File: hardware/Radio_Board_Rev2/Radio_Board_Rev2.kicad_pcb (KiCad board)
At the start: 2 copper layers, 100 x 65.5 mm, 20 parts, among them IC1 MAX7219CNG, J1 Conn_01x02_Socket, SW1 SW_DIP_x01, SW2 SW_DIP_x01, SW3 SW_DIP_x01, U1 ESP32-DEVKIT-V1, U3 MIC5219-3.3YM5

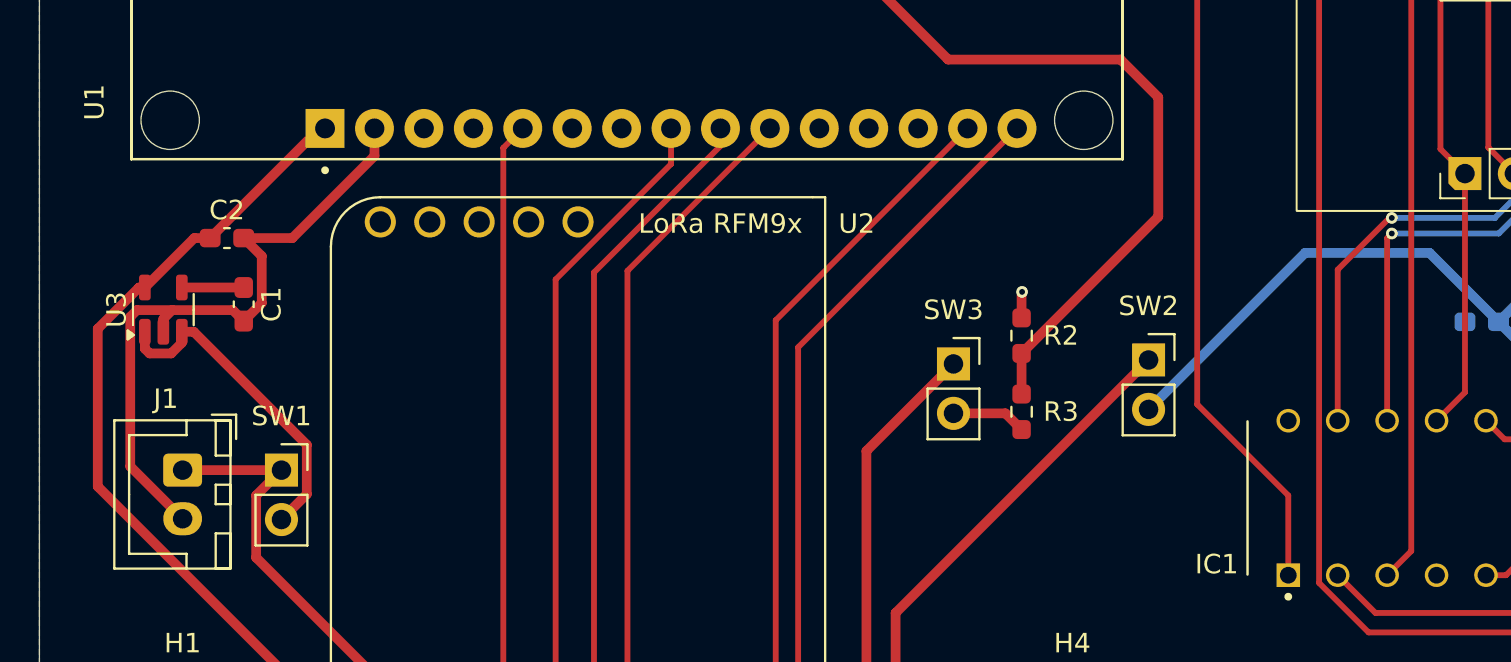
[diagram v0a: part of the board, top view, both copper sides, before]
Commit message: Add datasheets
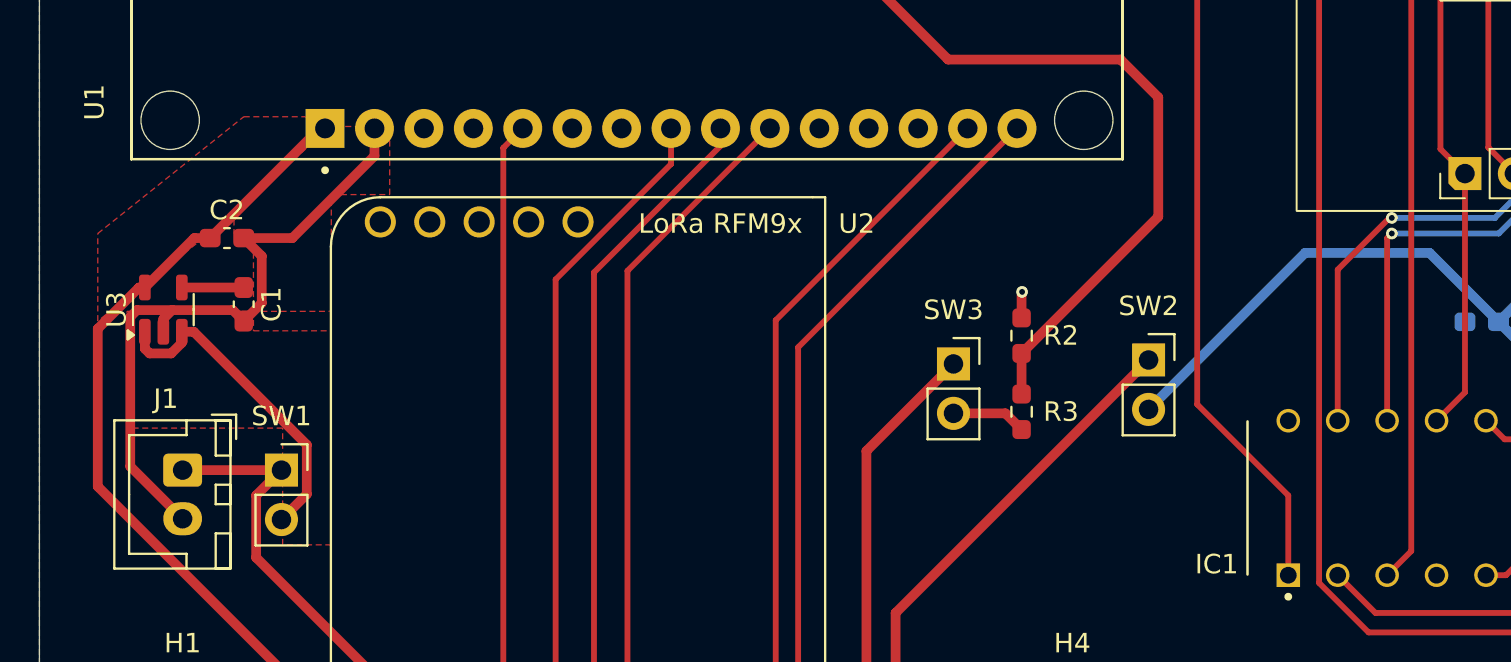
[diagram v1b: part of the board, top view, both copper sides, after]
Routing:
- added copper zone on F.Cu, net 3v3
- added copper zone on F.Cu, net GND
- added copper zone on F.Cu, net Vreg
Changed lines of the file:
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@@
 		)
 		(property "Value" "SW_DIP_x01"
-			(at 6.18 44.17 0)
+			(at -0.975 5.2975 0)
 			(layer "F.Fab")
 			(effects
@@
 	)
 	(segment
-		(start 148.26 134.62)
+		(start 148.5 125)
 		(end 148.26 125.24)
 		(width 0.3)
@@
 	(segment
 		(start 148.26 125.24)
-		(end 148.5 125)
+		(end 148.26 134.62)
 		(width 0.3)
 		(layer "F.Cu")
@@
 	)
 	(segment
-		(start 148.5 125)
-		(end 154 125)
+		(start 154 125)
+		(end 157.08 121.92)
 		(width 0.3)
 		(layer "B.Cu")
@@
 	)
 	(segment
-		(start 157.08 121.92)
-		(end 157.34 121.92)
+		(start 148.5 125)
+		(end 154 125)
 		(width 0.3)
 		(layer "B.Cu")
@@
 	)
 	(segment
-		(start 154 125)
-		(end 157.08 121.92)
+		(start 157.08 121.92)
+		(end 157.34 121.92)
 		(width 0.3)
 		(layer "B.Cu")
@@
 	)
 	(zone
+		(net 2)
+		(net_name "GND")
+		(layer "F.Cu")
+		(hatch edge 0.5)
+		(priority 4)
+		(connect_pads
+			(clearance 0.5)
+		)
+		(min_thickness 0.25)
+		(filled_areas_thickness no)
+		(fill yes
+			(thermal_gap 0.5)
+			(thermal_bridge_width 0.5)
+		)
+		(polygon
+			(pts
+				(xy 90 130) (xy 94 130) (xy 94 123) (xy 97 123) (xy 97 119.5) (xy 93.5 119.5) (xy 89 123.785714)
+				(xy 89 125) (xy 90 125)
+			)
+		)
+	)
+	(zone
+		(net 3)
+		(net_name "3v3")
+		(layer "F.Cu")
+		(hatch edge 0.5)
+		(priority 3)
+		(connect_pads
+			(clearance 0.5)
+		)
+		(min_thickness 0.25)
+		(filled_areas_thickness no)
+		(fill yes
+			(thermal_gap 0.5)
+			(thermal_bridge_width 0.5)
+		)
+		(polygon
+			(pts
+				(xy 82 129.5) (xy 82 125) (xy 82 125) (xy 89.5 119) (xy 94.5 119) (xy 89 124)
+			)
+		)
+	)
+	(zone
+		(net 29)
+		(net_name "Vreg")
+		(layer "F.Cu")
+		(hatch edge 0.5)
+		(priority 1)
+		(connect_pads
+			(clearance 0.5)
+		)
+		(min_thickness 0.25)
+		(filled_areas_thickness no)
+		(fill yes
+			(thermal_gap 0.5)
+			(thermal_bridge_width 0.5)
+		)
+		(polygon
+			(pts
+				(xy 83.5 129) (xy 94 129) (xy 94 141) (xy 91.5 141) (xy 91.5 135) (xy 83.5 135)
+			)
+		)
+	)
+	(zone
